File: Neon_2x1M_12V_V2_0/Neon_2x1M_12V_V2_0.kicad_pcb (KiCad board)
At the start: 2 copper layers, 77.5 x 51.5 mm, 35 parts, among them J2 Barrel_Jack_MountingPin, J4 Barrel_Jack_MountingPin, J5 Barrel_Jack_MountingPin, J6 Conn_01x03_Pin, Q1 IRLML2502TRPBF, Q2 IRLML2502TRPBF, SW1 SW_Push, SW2 SW_Push, U1 ESP32-WROOM-32, U3 LM2596T-ADJ

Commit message: updated schematic and layout for V2.0
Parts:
- removed G*** (x3): LOGO, LOGO
- removed J4, J5: Barrel_Jack_MountingPin, Connector_BarrelJack:BarrelJack_Horizontal
- added J7: Screw_Terminal_01x02, Connector_JST:JST_NV_B02P-NV_1x02_P5.00mm_Vertical, F.Cu at (214.1, 105.0)
- added J8: Screw_Terminal_01x02, Connector_JST:JST_NV_B02P-NV_1x02_P5.00mm_Vertical, F.Cu at (214.1, 120.0)
- moved J2 122.4 mm to (206.5, 138.5), turned to 180 degrees
- moved H1 114.3 mm to (164.5, 148.0)
- moved C1 112.0 mm to (198.5, 144.9), turned to -90 degrees
- moved L1 108.0 mm to (179.0, 140.0), turned to 180 degrees
- moved H4 102.3 mm to (214.5, 95.5)
- moved C3 88.8 mm to (168.5, 128.5), turned to 180 degrees
- moved D2 88.7 mm to (190.5, 144.5), turned to -90 degrees
- moved C4 84.9 mm to (169.0, 136.0), turned to 180 degrees
- moved U3 84.2 mm to (195.2, 137.7), turned to 90 degrees
- moved C2 82.6 mm to (198.0, 136.0), turned to 90 degrees
- moved H2 78.8 mm to (164.5, 95.5)
- moved H3 78.7 mm to (214.5, 148.0)
- moved R9 74.0 mm to (195.4, 126.7)
- moved R10 71.7 mm to (189.9, 126.7)
- moved R2 71.1 mm to (194.5, 112.0)
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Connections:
- net Net-(D2-K) renamed /BUCK_SW
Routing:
- net +12V: track 192.4 -> 0.00 mm, vias 7 -> 0
- net +3V3: track 51.9 -> 74.9 mm, vias 2 -> 0
- net ESP_EN: track 27.5 -> 6.59 mm, vias 2 -> 0
- net B_Jack: track 30.3 -> 14.0 mm, vias 3 -> 0
- net Net-(Q1-G): track 20.1 -> 6.19 mm
- net Net-(U3-FB): track 0.00 -> 8.32 mm
- net P_Jack: track 19.4 -> 11.8 mm, vias 1 -> 0
- net ESP_IO19: track 9.13 -> 5.62 mm
- net ESP_IO0: track 12.5 -> 9.46 mm
- net ESP_U0TX: track 10.7 -> 13.7 mm
- net Net-(D9-A): track 0.00 -> 2.96 mm
- net ESP_U0RX: track 13.7 -> 16.6 mm
- net ESP_IO18: track 6.80 -> 5.59 mm
- net ESP_IO2: track 6.38 -> 5.20 mm
- net Net-(D5-A): track 3.52 -> 2.46 mm
- added copper zone on F.Cu, net +12V
- added copper zone on F.Cu, net +3V3
- added copper zone on F.Cu, net /BUCK_SW
- removed copper zone on B.Cu, net GND
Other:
- board size 77.5 x 51.5 mm -> 60 x 59.5 mm
- board text removed: "E Adel"
- board text removed: "Made on Earth by pharaohs"

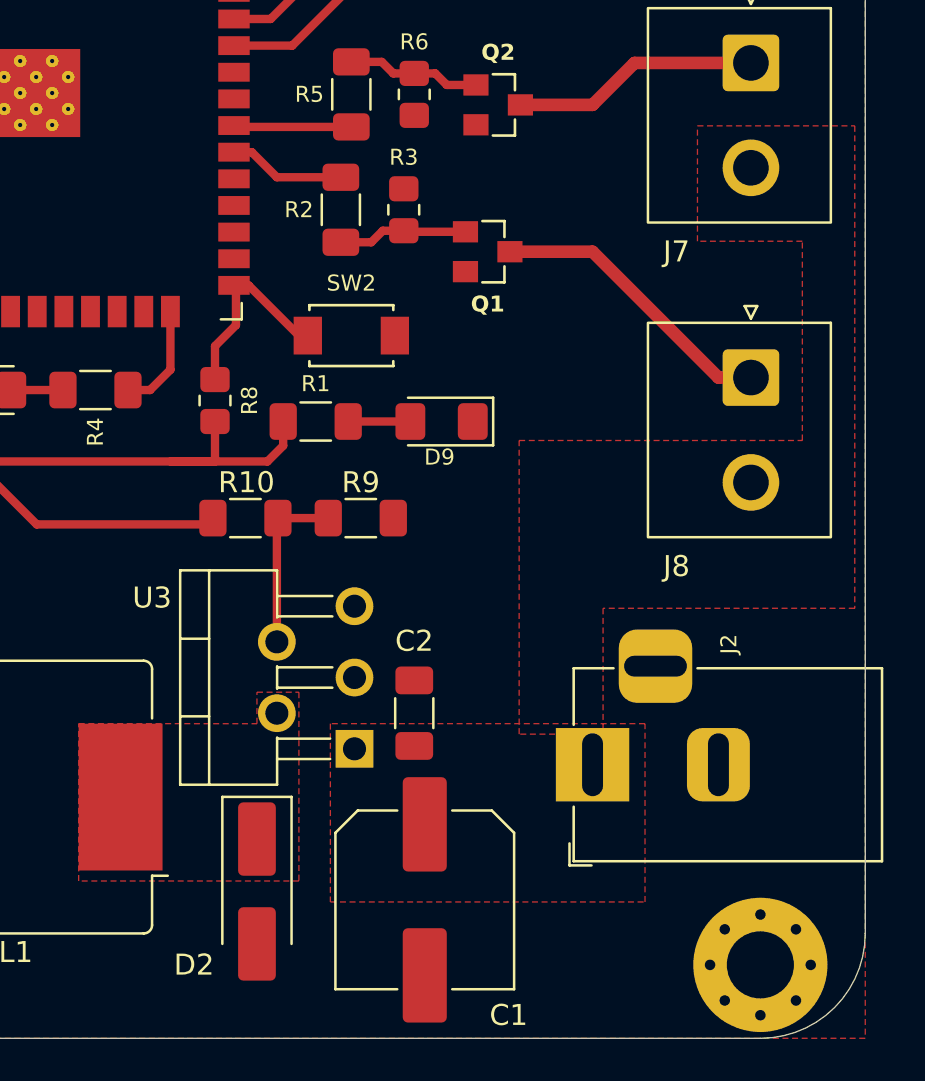
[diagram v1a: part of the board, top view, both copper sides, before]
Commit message: updated placement, routing and added final touches
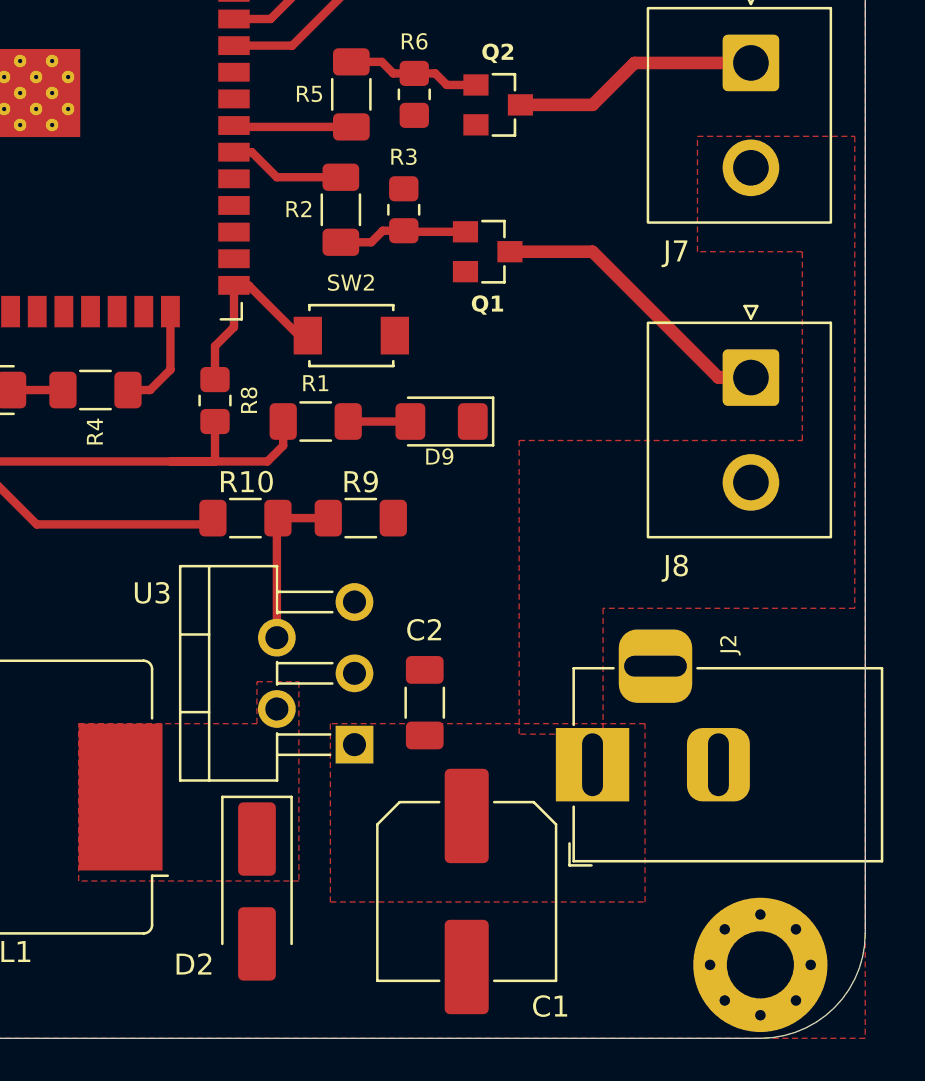
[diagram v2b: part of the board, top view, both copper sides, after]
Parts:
- moved C1 2.04 mm to (200.5, 144.5)
- moved C2 0.71 mm to (198.5, 135.5)
- moved U3 0.20 mm to (195.2, 137.5)
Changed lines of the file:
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@@
 		(capping no)
 		(filling no)
-		(zone_defaults)
 		(aux_axis_origin 159.5 92)
 		(grid_origin 159.5 92)
@@
 	(footprint "Capacitor_SMD:C_1206_3216Metric_Pad1.33x1.80mm_HandSolder"
 		(layer "F.Cu")
-		(at 198 136 90)
+		(at 198.5 135.5 90)
 		(descr "Capacitor SMD 1206 (3216 Metric), square (rectangular) end terminal, IPC-7351 nominal with elongated pad for handsoldering. (Body size source: IPC-SM-782 page 76, https://www.pcb-3d.com/wordpress/wp-content/uploads/ipc-sm-782a_amendment_1_and_2.pdf)")
 		(tags "capacitor handsolder")
@@
 	(footprint "Package_TO_SOT_THT:TO-220-5_P3.4x3.7mm_StaggerOdd_Lead3.8mm_Vertical"
 		(layer "F.Cu")
-		(at 195.15 137.7 90)
+		(at 195.15 137.5 90)
 		(descr "TO-220-5, Vertical, RM 1.7mm, Pentawatt, staggered type-1, see http://www.analog.com/media/en/package-pcb-resources/package/pkg_pdf/ltc-legacy-to-220/to-220_5_05-08-1421.pdf?domain=www.linear.com, https://www.diodes.com/assets/Package-Files/TO220-5.pdf")
 		(tags "TO-220-5 Vertical RM 1.7mm Pentawatt staggered type-1")
@@
 	(footprint "Capacitor_SMD:C_Elec_8x10.2"
 		(layer "F.Cu")
-		(at 198.5 144.9 -90)
+		(at 200.5 144.5 -90)
 		(descr "SMD capacitor, aluminum electrolytic nonpolar, 8.0x10.2mm")
 		(tags "capacitor electrolytic nonpolar")
@@
 			(net "GND")
 			(pintype "passive")
+			(thermal_bridge_width 2)
 		)
 		(pad "3" thru_hole roundrect
@@
 	)
 	(segment
+		(start 206.5 114)
+		(end 202.56 114)
+		(width 0.6)
+		(layer "F.Cu")
+		(net "B_Jack")
+	)
+	(segment
+		(start 214.05 120)
+		(end 212.5 120)
+		(width 0.6)
+		(layer "F.Cu")
+		(net "B_Jack")
+	)
+	(segment
+		(start 212.5 120)
+		(end 206.5 114)
+		(width 0.6)
+		(layer "F.Cu")
+		(net "B_Jack")
+	)
+	(segment
 		(start 189.405 104.175)
 		(end 192.182995 104.175)
@@
 	)
 	(segment
-		(start 191.5 126.7)
-		(end 193.9 126.7)
+		(start 191.45 132.4)
+		(end 191.45 126.75)
 		(width 0.4)
 		(layer "F.Cu")
@@
 	)
 	(segment
-		(start 191.45 132.6)
-		(end 191.45 126.75)
+		(start 191.5 126.7)
+		(end 193.9 126.7)
 		(width 0.4)
 		(layer "F.Cu")
@@
 	)
 	(segment
-		(start 206.5 114)
-		(end 202.56 114)
-		(width 0.6)
-		(layer "F.Cu")
-		(net "B_Jack")
-	)
-	(segment
-		(start 214.05 120)
-		(end 212.5 120)
-		(width 0.6)
-		(layer "F.Cu")
-		(net "B_Jack")
-	)
-	(segment
-		(start 212.5 120)
-		(end 206.5 114)
-		(width 0.6)
-		(layer "F.Cu")
-		(net "B_Jack")
-	)
-	(segment
-		(start 206.5 107)
-		(end 203.06 107)
-		(width 0.6)
-		(layer "F.Cu")
-		(net "P_Jack")
-	)
-	(segment
-		(start 208.5 105)
-		(end 206.5 107)
-		(width 0.6)
-		(layer "F.Cu")
-		(net "P_Jack")
-	)
-	(segment
-		(start 214.05 105)
-		(end 208.5 105)
-		(width 0.6)
-		(layer "F.Cu")
-		(net "P_Jack")
-	)
-	(segment
 		(start 170 102)
 		(end 168.5 102)
@@
 	)
 	(segment
+		(start 206.5 107)
+		(end 203.06 107)
+		(width 0.6)
+		(layer "F.Cu")
+		(net "P_Jack")
+	)
+	(segment
+		(start 208.5 105)
+		(end 206.5 107)
+		(width 0.6)
+		(layer "F.Cu")
+		(net "P_Jack")
+	)
+	(segment
+		(start 214.05 105)
+		(end 208.5 105)
+		(width 0.6)
+		(layer "F.Cu")
+		(net "P_Jack")
+	)
+	(segment
 		(start 186.375 119.625)
 		(end 185.405 120.595)
@@
 	)
 	(segment
-		(start 188.5 118.5)
-		(end 189.5 117.5)
+		(start 189.405 117.595)
+		(end 189.405 115.605)
 		(width 0.4)
 		(layer "F.Cu")
@@
 	)
 	(segment
-		(start 189.5 115.7)
-		(end 189.405 115.605)
+		(start 192.5 118)
+		(end 190.105 115.605)
 		(width 0.4)
 		(layer "F.Cu")
@@
 	)
 	(segment
-		(start 189.5 117.5)
-		(end 189.5 115.7)
+		(start 188.5 118.5)
+		(end 189.405 117.595)
 		(width 0.4)
 		(layer "F.Cu")
@@
 		(net "ESP_IO0")
 	)
-	(segment
-		(start 192.5 118)
-		(end 190.105 115.605)
-		(width 0.4)
-		(layer "F.Cu")
-		(net "ESP_IO0")
-	)
 	(zone
 		(net "/BUCK_SW")
@@
 		(polygon
 			(pts
-				(xy 182.003625 136.498068) (xy 190.5 136.502176) (xy 190.5 135) (xy 192.5 135) (xy 192.5 144) (xy 182 144)
+				(xy 182.003625 136.498068) (xy 190.5 136.502176) (xy 190.5 134.5) (xy 192.5 134.5) (xy 192.5 144)
+				(xy 182 144)
 			)
 		)
@@
 		(polygon
 			(pts
-				(xy 203 137) (xy 203 123) (xy 216.5 123) (xy 216.5 113.5) (xy 211.5 113.5) (xy 211.5 108) (xy 219 108)
+				(xy 203 137) (xy 203 123) (xy 216.5 123) (xy 216.5 114) (xy 211.5 114) (xy 211.5 108.5) (xy 219 108.5)
 				(xy 219 131) (xy 207 131) (xy 207 137)
 			)

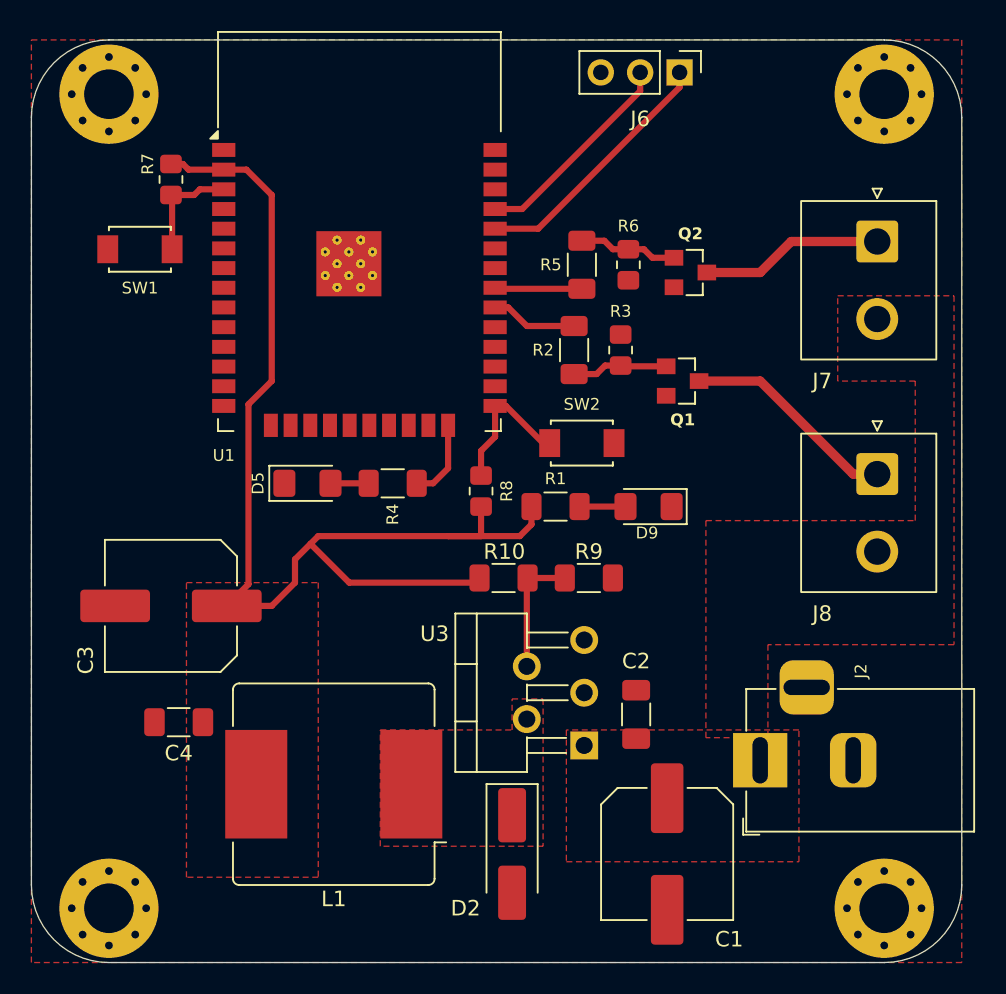
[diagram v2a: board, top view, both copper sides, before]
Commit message: updated BOM and generated BOM csv file also updated schematic and layout along
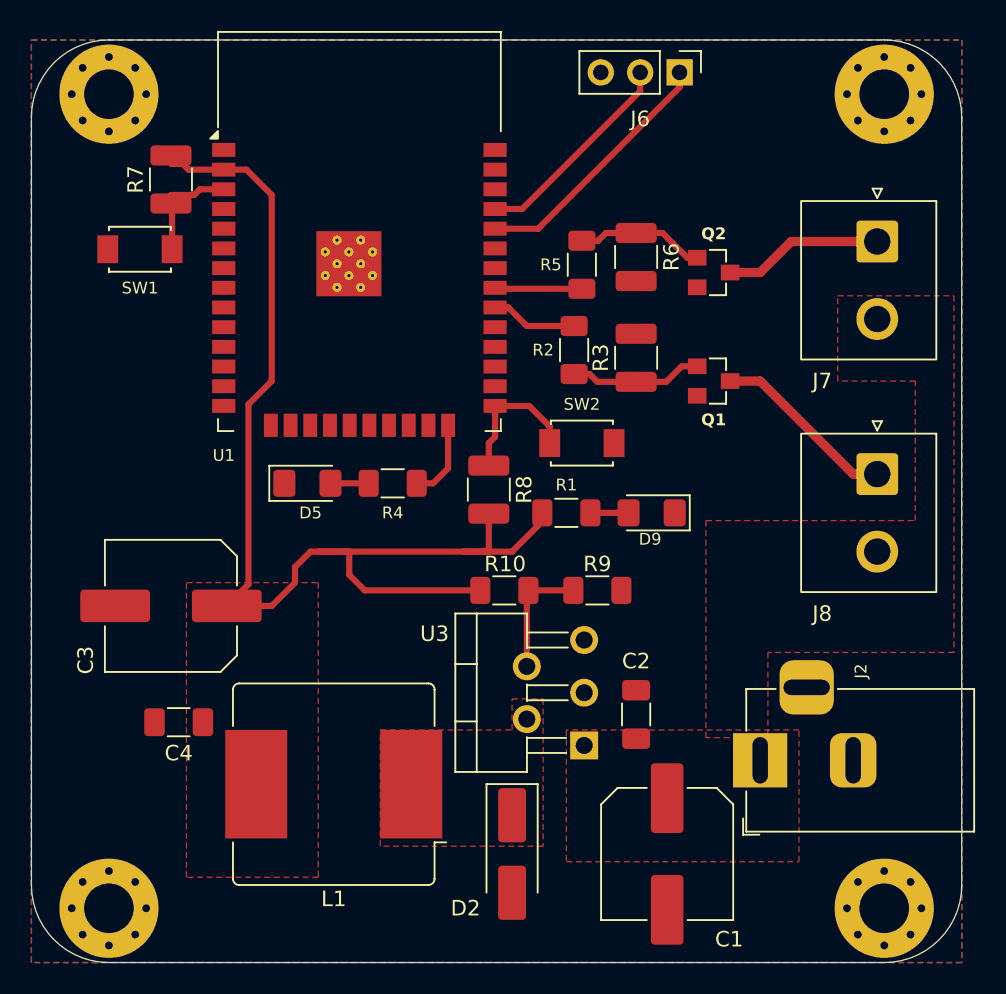
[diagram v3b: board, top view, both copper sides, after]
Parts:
- D5: value Red Indicator LED -> Blue Indicator LED
- R3, R6, R7, R8: footprint Resistor_SMD:R_0805_2012Metric_Pad1.20x1.40mm_HandSolder -> Resistor_SMD:R_1210_3225Metric_Pad1.30x2.65mm_HandSolder
- R9: value 1.3K -> 16K
- moved Q1 2.00 mm to (203.5, 114.0)
- moved Q2 1.50 mm to (203.5, 107.0)
- moved R3 1.12 mm to (198.5, 112.5)
- moved R9 0.97 mm to (196.0, 127.5)
- moved R1 0.81 mm to (194.0, 122.5)
- moved R10 0.80 mm to (190.0, 127.5)
- moved R6 0.71 mm to (198.5, 106.0)
- moved R8 0.51 mm to (189.0, 121.0)
- moved D9 0.45 mm to (199.5, 122.5)
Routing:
- net Net-(Q1-G): track 6.19 -> 8.56 mm
- net B_Jack: track 14.0 -> 12.0 mm
- net Net-(Q2-G): track 6.40 -> 8.31 mm
- net P_Jack: track 11.8 -> 10.3 mm
- net Net-(D9-A): track 2.96 -> 2.26 mm
- added copper zone on B.Cu, net GND

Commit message: generated BOM
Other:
- board text added: "+12V"
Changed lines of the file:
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@@
 		(tags "connector JST NV vertical")
 		(property "Reference" "J8"
-			(at 9 3.55 180)
+			(at 5 6.55 180)
 			(layer "F.SilkS")
 			(effects
@@
 		(tags "connector JST NV vertical")
 		(property "Reference" "J7"
-			(at 9 3.55 180)
+			(at 5.5 6.55 180)
 			(layer "F.SilkS")
 			(effects
@@
 		(layer "Edge.Cuts")
 	)
+	(gr_text "+12V"
+		(at 214 114.5 0)
+		(layer "F.SilkS")
+		(effects
+			(font
+				(size 1 1)
+				(thickness 0.25)
+				(bold yes)
+			)
+			(justify left bottom)
+		)
+	)
+	(gr_text "+12V"
+		(at 214 129.5 0)
+		(layer "F.SilkS")
+		(effects
+			(font
+				(size 1 1)
+				(thickness 0.25)
+				(bold yes)
+			)
+			(justify left bottom)
+		)
+	)
 	(gr_text_box "Metanoio Design Rules :\n\n- Minimum clearance: 0.4mm\n- Minimum track width: 0.4mm\n- Minimum via diameter: 1.4mm\n- Minimum via hole: 0.6mm\n- Max Dimensions: 20x29 cm"

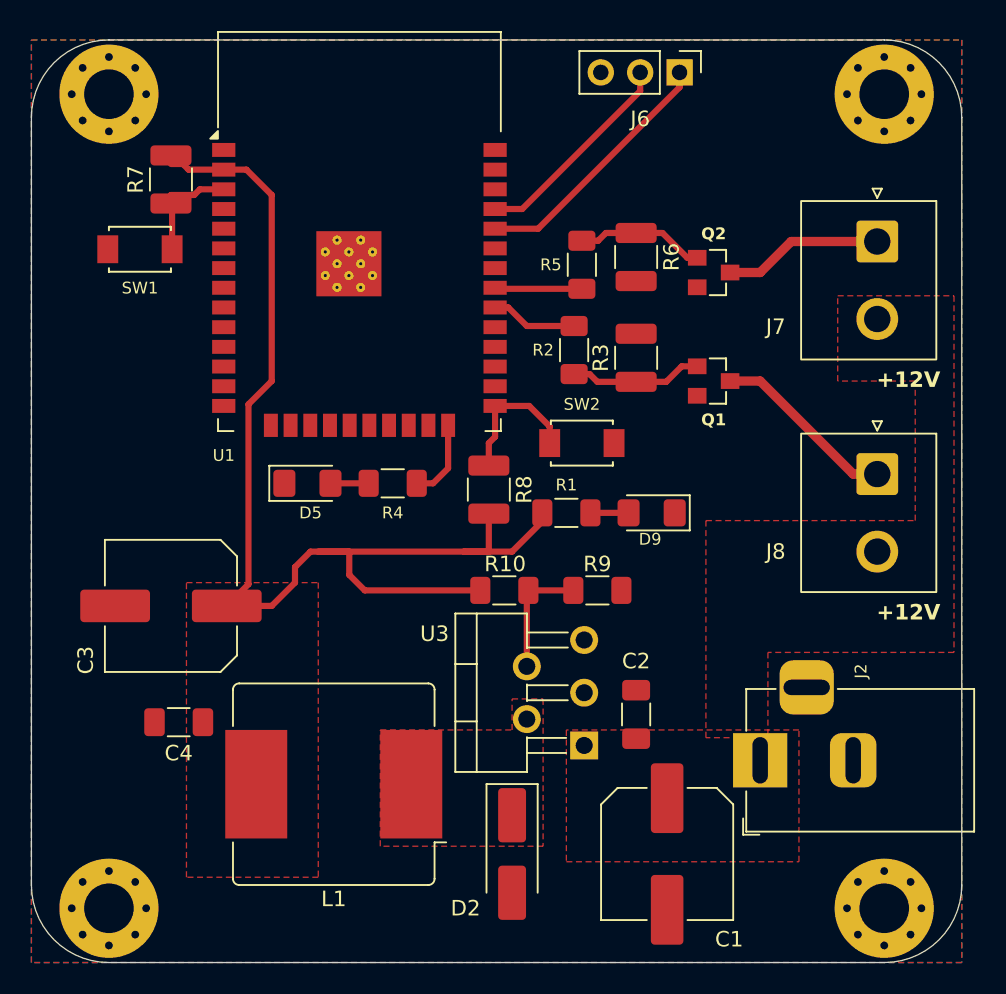
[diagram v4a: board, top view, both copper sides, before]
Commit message: updated production files and updated connectors orientation to match 1 layer pcb manufacturing as connectors flipped
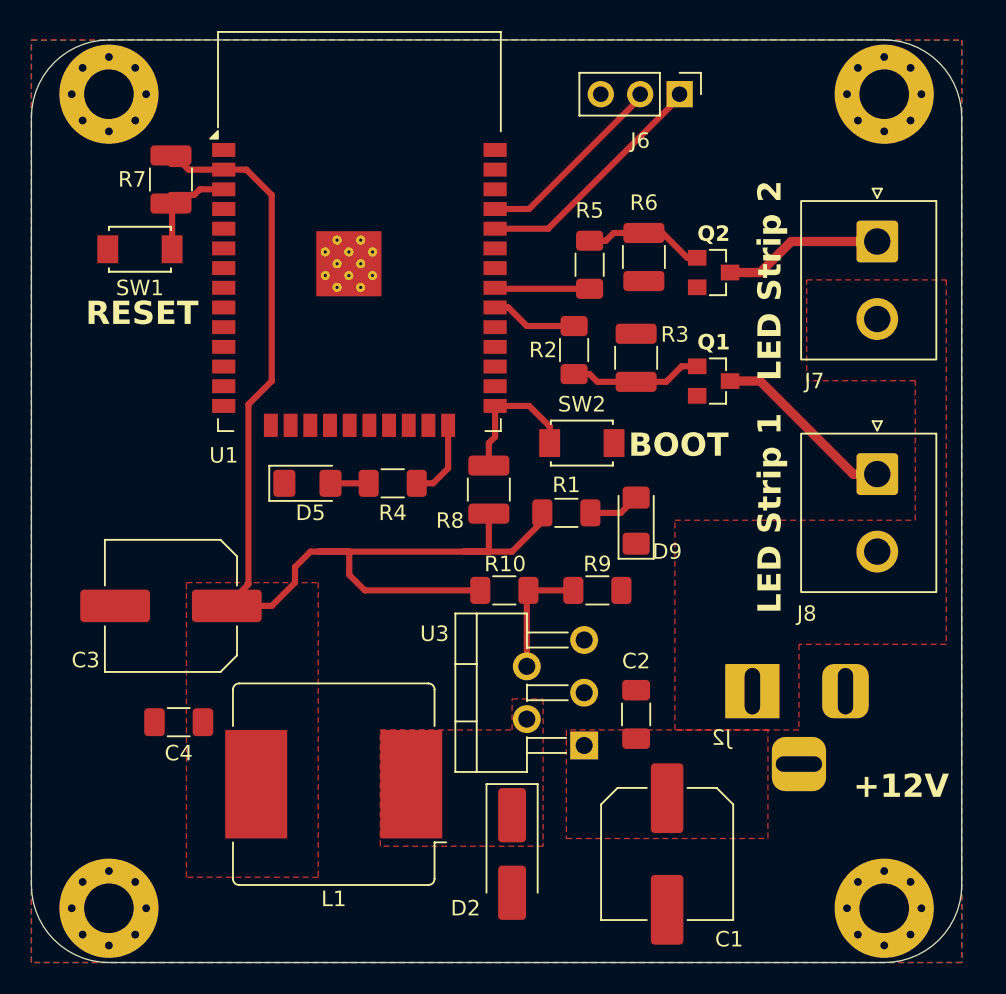
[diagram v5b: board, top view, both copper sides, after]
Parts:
- J2: moved to B.Cu
- moved J2 4.49 mm to (206.0, 134.0)
- moved J6 1.41 mm to (201.3, 95.5)
- moved D9 1.12 mm to (198.5, 123.0), turned to 90 degrees
- moved R5 0.50 mm to (195.5, 106.5)
- moved R6 0.50 mm to (199.0, 106.0)
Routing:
- net ESP_U0TX: track 13.7 -> 12.6 mm
- net Net-(D9-A): track 2.26 -> 3.36 mm
- net ESP_U0RX: track 16.6 -> 15.6 mm
- net Net-(Q2-G): track 8.31 -> 7.81 mm
- net ESP_IO19: track 5.62 -> 6.12 mm
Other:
- board text added: "+"
- board text added: "-"
- board text added: "BOOT"
- board text added: "LED Strip 1"
- board text added: "LED Strip 2"
- board text added: "RESET"
